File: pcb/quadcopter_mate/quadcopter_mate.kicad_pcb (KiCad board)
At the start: 2 copper layers, 48.3 x 73.7 mm, 10 parts, among them J1 RJ45

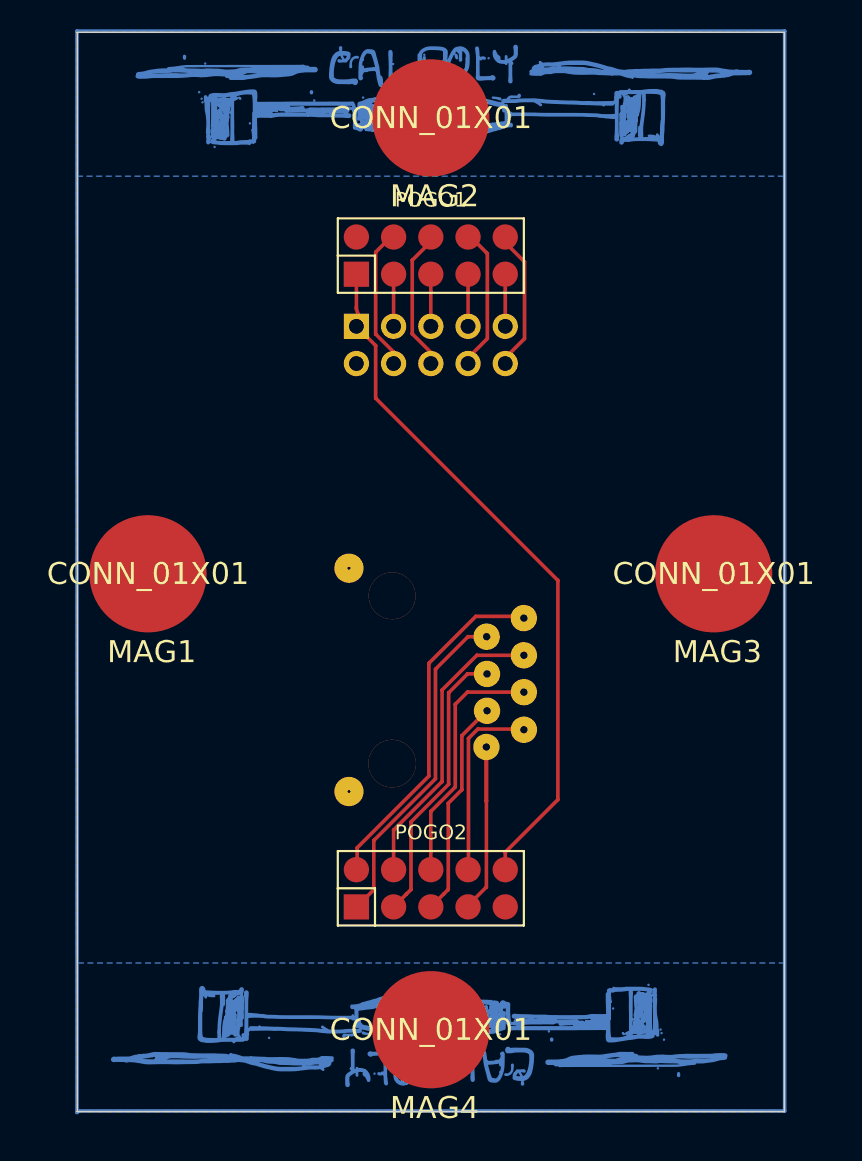
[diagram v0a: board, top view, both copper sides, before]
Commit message: Mirrored text in mate board to be correct when gerber is mirrored
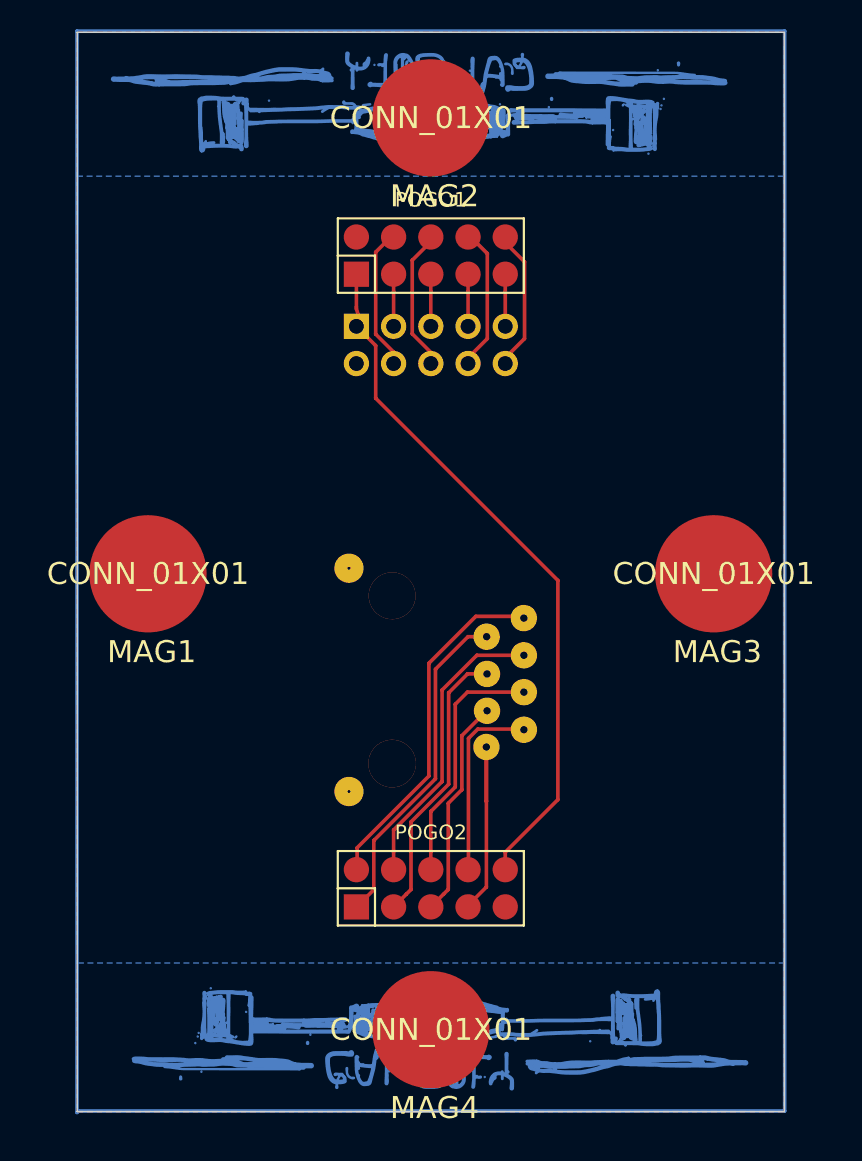
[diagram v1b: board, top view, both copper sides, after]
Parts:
- removed the G*** at (228.9, 62.0)
- removed the G*** at (227.5, 124.2)
- added G***: LOGO, quadcopter_footprints:logo_mirror, B.Cu at (228.7, 124.4)
- added G***: LOGO, quadcopter_footprints:logo_mirror, B.Cu at (227.5, 62.4)

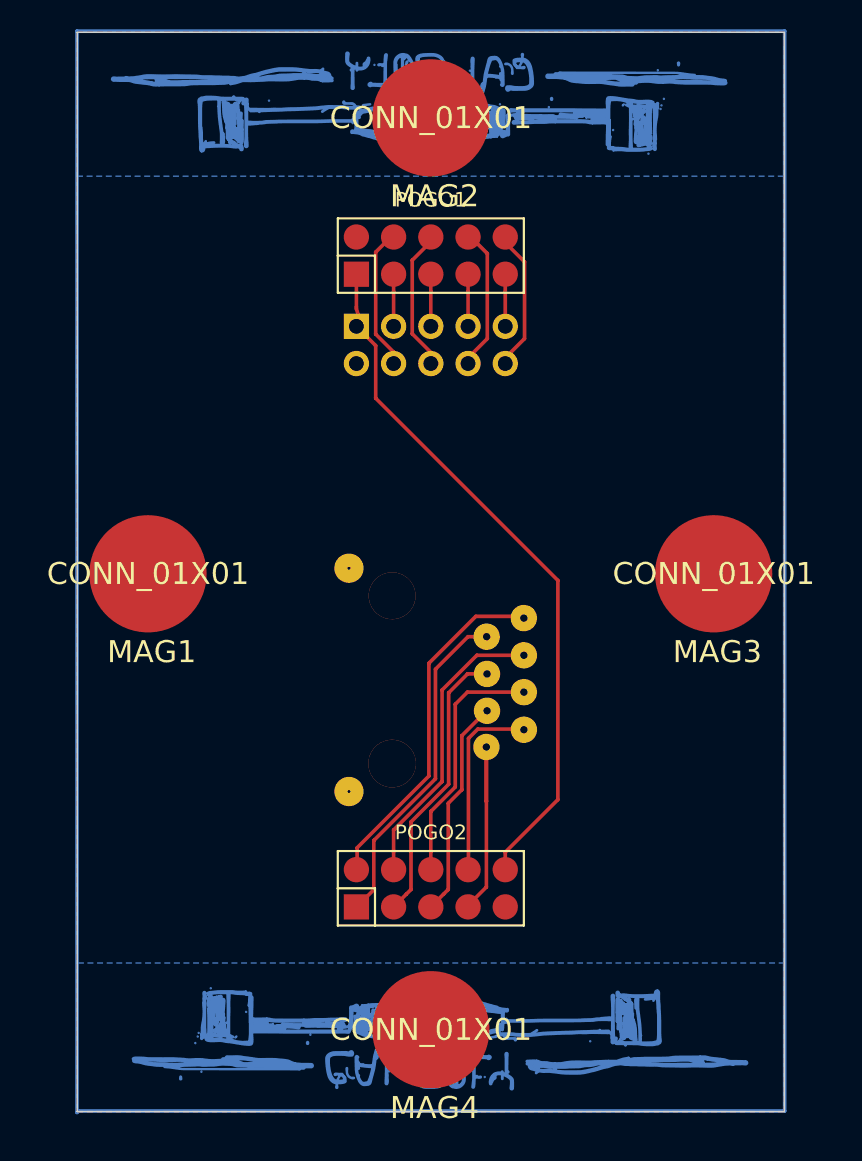
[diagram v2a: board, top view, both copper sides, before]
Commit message: Reformatted schematics
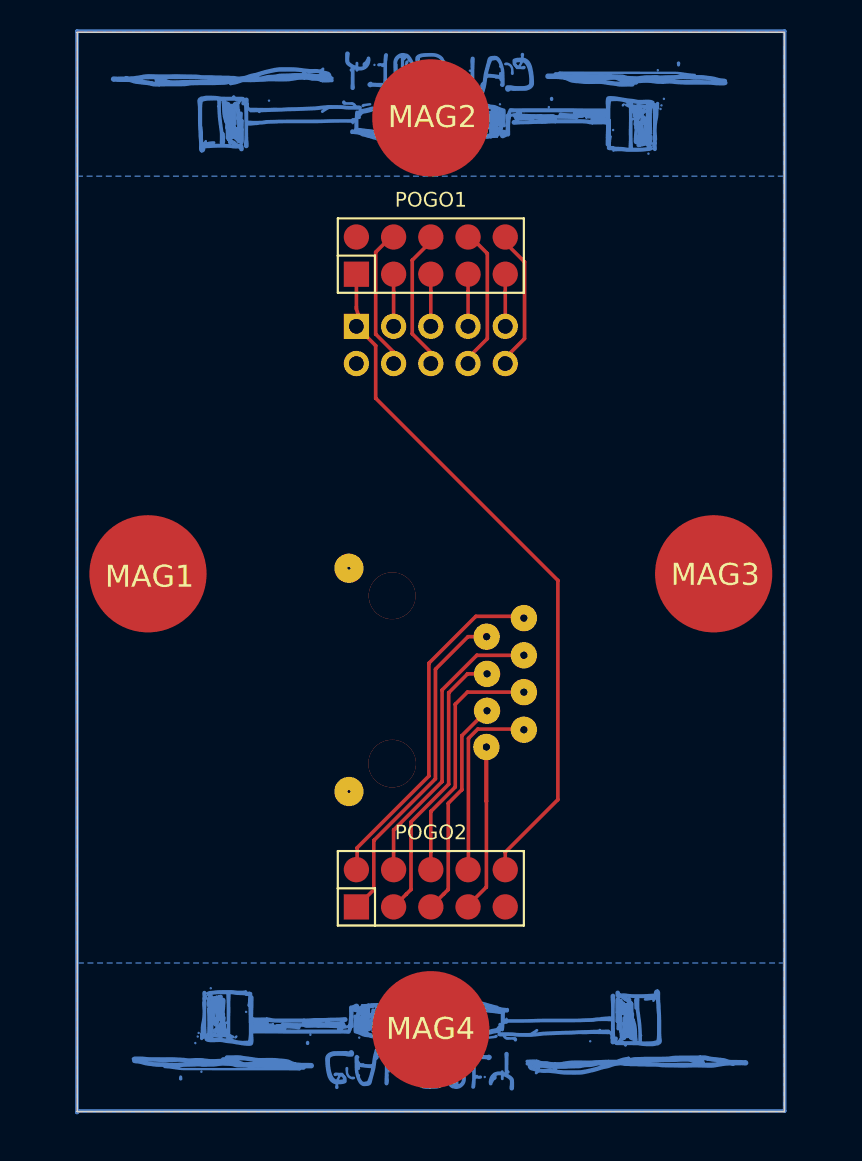
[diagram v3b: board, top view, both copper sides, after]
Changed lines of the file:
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@@
-(kicad_pcb (version 4) (host pcbnew "(after 2015-mar-04 BZR unknown)-product")
+(kicad_pcb (version 4) (host pcbnew "(after 2015-may-25 BZR unknown)-product")
   (general
     (links 26)
     (no_connects 0)
-    (area 203.989999 56.619999 252.350001 130.380001)
+    (area 201.341001 56.264999 254.999 130.715002)
     (thickness 1.6)
     (drawings 6)
@@
       (padsonsilk false)
       (subtractmaskfromsilk false)
-      (outputformat 1)
+      (outputformat 5)
       (mirror false)
       (drillshape 0)
@@
     (descr "Through hole pin header")
     (tags "pin header")
-    (fp_text reference HEADER1 (at 0 5.1 270) (layer B.SilkS)
+    (fp_text reference HEADER1 (at 5.267 -5.06 360) (layer B.SilkS)
       (effects (font (size 1 1) (thickness 0.15)) (justify mirror))
     )
@@
   (module quadcopter_footprints:8mmMagnet locked (layer F.Cu)
     (at 208.866 93.627)
-    (fp_text reference MAG1 (at 0.254 5.334) (layer F.SilkS)
+    (fp_text reference MAG1 (at 0.107 0.187) (layer F.SilkS)
       (effects (font (size 1.5 1.5) (thickness 0.15)))
     )
-    (fp_text value CONN_01X01 (at 0 0) (layer F.SilkS)
+    (fp_text value CONN_01X01 (at 0 0) (layer F.SilkS) hide
       (effects (font (size 1.5 1.5) (thickness 0.15)))
     )
@@
   (module quadcopter_footprints:8mmMagnet locked (layer F.Cu)
     (at 228.17 62.512)
-    (fp_text reference MAG2 (at 0.254 5.334) (layer F.SilkS)
+    (fp_text reference MAG2 (at 0.107 -0.067) (layer F.SilkS)
       (effects (font (size 1.5 1.5) (thickness 0.15)))
     )
-    (fp_text value CONN_01X01 (at 0 0) (layer F.SilkS)
+    (fp_text value CONN_01X01 (at 0 0) (layer F.SilkS) hide
       (effects (font (size 1.5 1.5) (thickness 0.15)))
     )
@@
   (module quadcopter_footprints:8mmMagnet locked (layer F.Cu)
     (at 247.474 93.627)
-    (fp_text reference MAG3 (at 0.254 5.334) (layer F.SilkS)
+    (fp_text reference MAG3 (at 0.107 0.06) (layer F.SilkS)
       (effects (font (size 1.5 1.5) (thickness 0.15)))
     )
-    (fp_text value CONN_01X01 (at 0 0) (layer F.SilkS)
+    (fp_text value CONN_01X01 (at 0 0) (layer F.SilkS) hide
       (effects (font (size 1.5 1.5) (thickness 0.15)))
     )
@@
   (module quadcopter_footprints:8mmMagnet locked (layer F.Cu)
     (at 228.17 124.742)
-    (fp_text reference MAG4 (at 0.254 5.334) (layer F.SilkS)
+    (fp_text reference MAG4 (at -0.02 -0.067) (layer F.SilkS)
       (effects (font (size 1.5 1.5) (thickness 0.15)))
     )
-    (fp_text value CONN_01X01 (at 0 0) (layer F.SilkS)
+    (fp_text value CONN_01X01 (at 0 0) (layer F.SilkS) hide
       (effects (font (size 1.5 1.5) (thickness 0.15)))
     )
@@
     (at 231.98 101.12 90)
     (tags RJ45)
-    (fp_text reference J1 (at -0.10668 5.3721 90) (layer B.SilkS)
+    (fp_text reference J1 (at -0.10668 5.3721 90) (layer B.SilkS) hide
       (effects (font (thickness 0.3048)) (justify mirror))
     )
-    (fp_text value RJ45 (at 0.3556 -12.1666 90) (layer B.SilkS)
+    (fp_text value RJ45 (at 0.321 -6.497 90) (layer B.SilkS)
       (effects (font (thickness 0.3048)) (justify mirror))
     )
